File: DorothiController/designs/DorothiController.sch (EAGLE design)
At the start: 27 parts

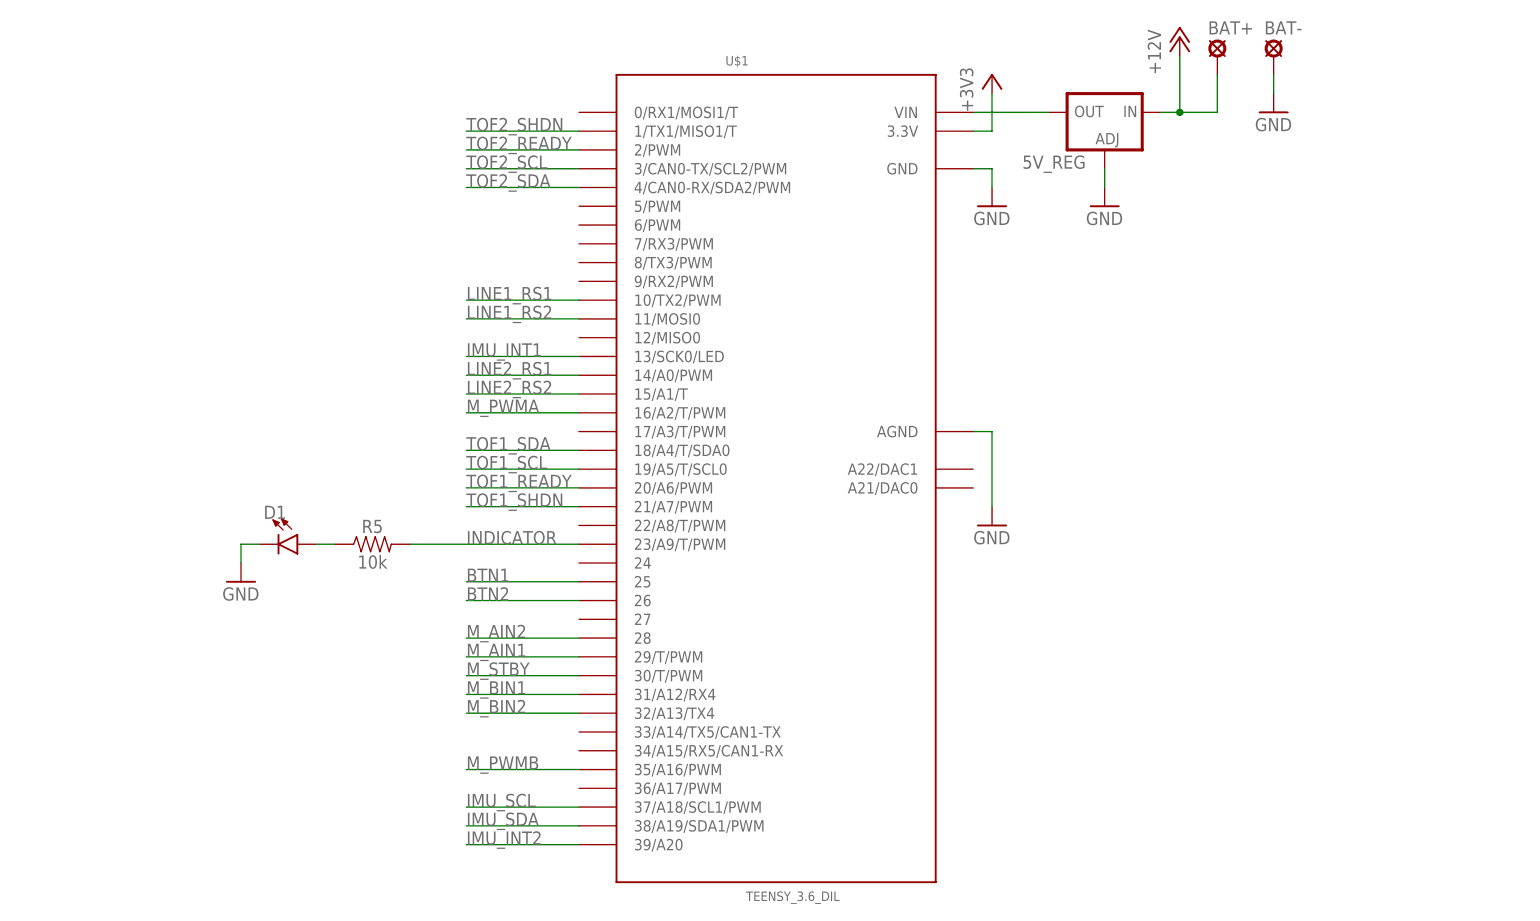
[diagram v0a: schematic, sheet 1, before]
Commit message: new 2 layer board with encoders
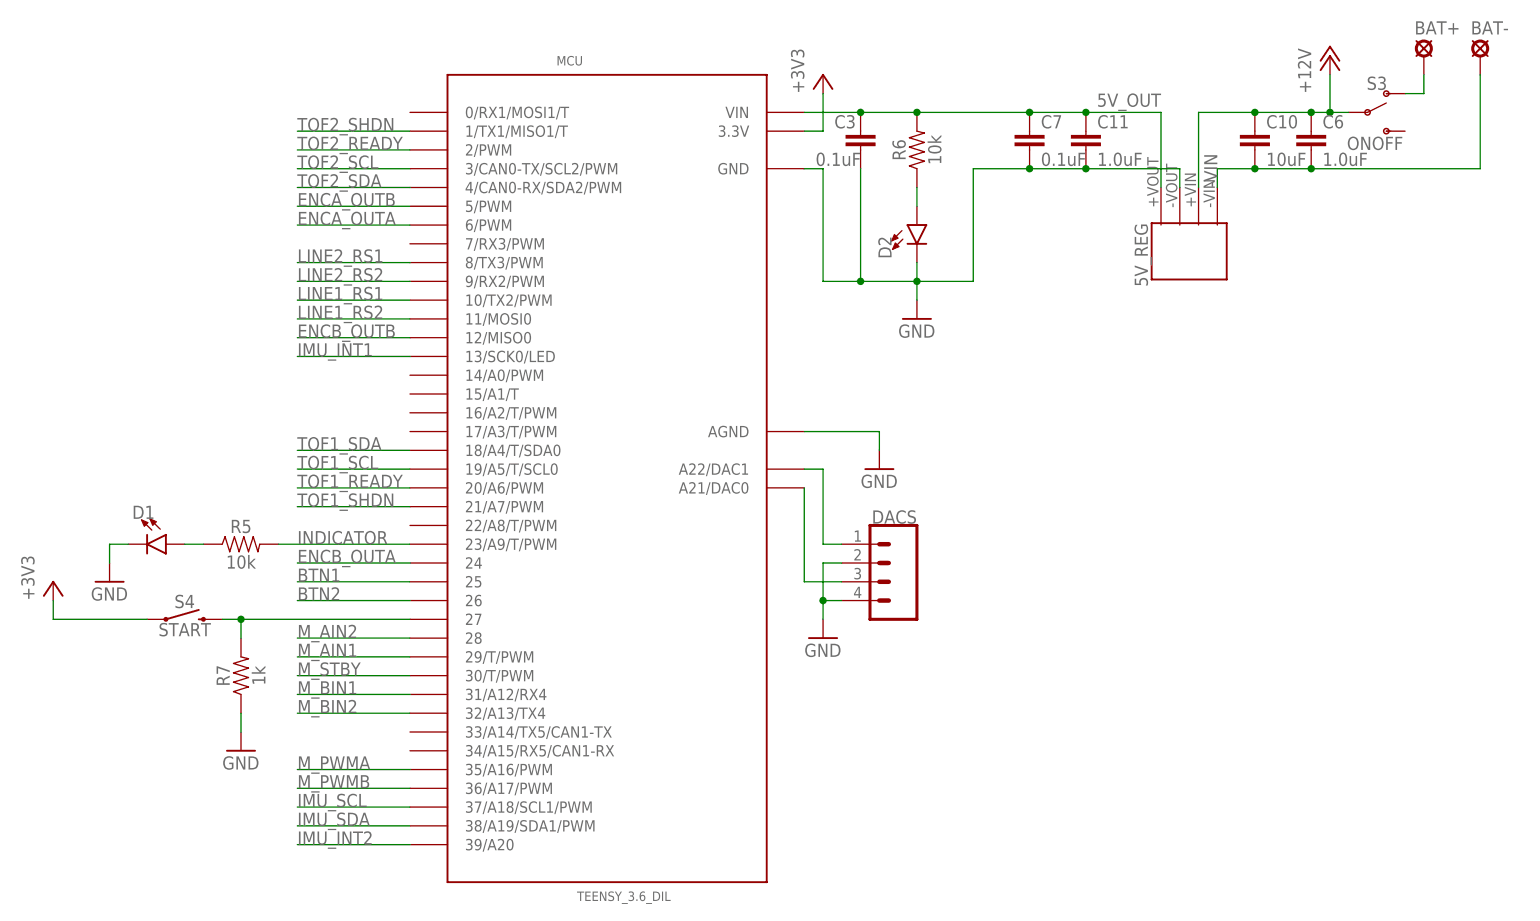
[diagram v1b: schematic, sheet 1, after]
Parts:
- removed U$1: TEENSY_3.6_DIL, Teensy_3_and_LC_Series_Boards_v1.4:TEENSY_3.6_DIL
- added C10: 10uF, SparkFun-Capacitors:10UF-0603-6.3V-20%
- added C11, C6: 1.0uF, SparkFun-Capacitors:1.0UF-0603-16V-10%
- added C13, C14: 10uF, SparkFun-Capacitors:10UF-POLAR-0603-6.3V-20%(TANT)
- added C7: 0.1uF, SparkFun-Capacitors:0.1UF-0603-25V-(+80/-20%)
- added C8, C9: 0.1uF, SparkFun-Capacitors:0.1UF-0603-25V-5%
- added D2: (no value), SparkFun-LED:LED0603
- added DACS: (no value), SparkFun-Connectors:CONN_04
- added ENCODERA, ENCODERB: (no value), SparkFun-Connectors:CONN_06SILK_FEMALE_PTH
- added MCU: TEENSY_3.6_DIL, Teensy_3_and_LC_Series_Boards_v1.4:TEENSY_3.6_DIL
- added R6: 10k, SparkFun-Resistors:10KOHM-0603-1/10W-1%
- added R7: 1k, SparkFun-Resistors:1KOHM-0603-1/10W-1%
- added S3: ONOFF, SparkFun-Switches:SWITCH-SPDT-PTH-11.6X4.0MM
- added S4: START, SparkFun-Switches:MOMENTARY-SWITCH-SPST-SMD-6.0X3.5MM
- 5V_REG: value (none) -> CRE1S1205SC; device v-reg:LM138-TL -> CRE1S1205SC:CRE1S1205SC
- C1: device SparkFun-Capacitors:10UF-POLAR-EIA3528-20V-10%(TANT) -> SparkFun-Capacitors:10UF-0603-6.3V-20%
- C3: value 10uF -> 0.1uF; device SparkFun-Capacitors:10UF-POLAR-EIA3528-20V-10%(TANT) -> SparkFun-Capacitors:0.1UF-0603-25V-(+80/-20%)
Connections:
- new net +VIN: BAT+.MP, S3.O
- new net -VIN: 5V_REG.-VIN, BAT-.MP, C10.2, C6.2
- new net DAC1: DACS.1, MCU.A22/DAC1
- new net DAC2: DACS.3, MCU.A21/DAC0
- new net ENCA_OUTA: ENCODERA.3, MCU.6/PWM
- new net ENCA_OUTB: ENCODERA.2, MCU.5/PWM
- new net ENCB_OUTA: ENCODERB.3, MCU.24
- new net ENCB_OUTB: ENCODERB.2, MCU.12/MISO0
- new net N$7: D2.A, R6.1
- new net START: MCU.27, R7.2, S4.2
- net +12V: now also 5V_REG.+VIN, C10.1, C13.+, C14.+, C6.1, S3.P; no longer 5V_REG.IN, BAT+.MP, C3.+, TB1.VM1
- net +3V3: now also C1.1, C8.1, C9.1, ENCODERA.4, ENCODERB.4, MCU.3.3V, S4.1; no longer C1.+, U$1.3.3V
- net 5V_OUT: now also 5V_REG.+VOUT, C11.1, C3.1, C7.1, MCU.VIN, R6.2; no longer 5V_REG.OUT, U$1.VIN
- net BTN1: now also MCU.25; no longer U$1.25
- net BTN2: now also MCU.26; no longer U$1.26
- net GND: now also 5V_REG.-VOUT, C1.2, C11.2, C13.-, C14.-, C3.2, C7.2, C8.2, C9.2, D2.C, DACS.2, DACS.4, ENCODERA.1, ENCODERB.1, MCU.AGND, MCU.GND, R7.1; no longer 5V_REG.ADJ, BAT-.MP, C1.-, C3.-, U$1.AGND, U$1.GND
- net IMU_INT1: now also MCU.13/SCK0/LED; no longer U$1.13/SCK0/LED
- net IMU_INT2: now also MCU.39/A20; no longer U$1.39/A20
- net IMU_SCL: now also MCU.37/A18/SCL1/PWM; no longer U$1.37/A18/SCL1/PWM
- net IMU_SDA: now also MCU.38/A19/SDA1/PWM; no longer U$1.38/A19/SDA1/PWM
- net INDICATOR: now also MCU.23/A9/T/PWM; no longer U$1.23/A9/T/PWM
- net LINE1_RS1: now also MCU.10/TX2/PWM; no longer U$1.10/TX2/PWM
- net LINE1_RS2: now also MCU.11/MOSI0; no longer U$1.11/MOSI0
- net LINE2_RS1: now also MCU.8/TX3/PWM; no longer U$1.14/A0/PWM
- net LINE2_RS2: now also MCU.9/RX2/PWM; no longer U$1.15/A1/T
- net MA+: now also ENCODERA.5
- net MA-: now also ENCODERA.6
- net MB+: now also ENCODERB.5
- net MB-: now also ENCODERB.6
- net M_AIN1: now also MCU.29/T/PWM; no longer U$1.29/T/PWM
- net M_AIN2: now also MCU.28; no longer U$1.28
- net M_BIN1: now also MCU.31/A12/RX4; no longer U$1.31/A12/RX4
- net M_BIN2: now also MCU.32/A13/TX4; no longer U$1.32/A13/TX4
- net M_PWMA: now also MCU.35/A16/PWM; no longer U$1.16/A2/T/PWM
- net M_PWMB: now also MCU.36/A17/PWM; no longer U$1.35/A16/PWM
- net M_STBY: now also MCU.30/T/PWM; no longer U$1.30/T/PWM
- net TOF1_READY: now also MCU.20/A6/PWM; no longer U$1.20/A6/PWM
- net TOF1_SCL: now also MCU.19/A5/T/SCL0; no longer U$1.19/A5/T/SCL0
- net TOF1_SDA: now also MCU.18/A4/T/SDA0; no longer U$1.18/A4/T/SDA0
- net TOF1_SHDN: now also MCU.21/A7/PWM; no longer U$1.21/A7/PWM
- net TOF2_READY: now also MCU.2/PWM; no longer U$1.2/PWM
- net TOF2_SCL: now also MCU.3/CAN0-TX/SCL2/PWM; no longer U$1.3/CAN0-TX/SCL2/PWM
- net TOF2_SDA: now also MCU.4/CAN0-RX/SDA2/PWM; no longer U$1.4/CAN0-RX/SDA2/PWM
- net TOF2_SHDN: now also MCU.1/TX1/MISO1/T; no longer U$1.1/TX1/MISO1/T
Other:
- moved on the sheet: BAT+, BAT-, C4, D1, LINE1, LINE2, R3, R4, R5, S1, S2
